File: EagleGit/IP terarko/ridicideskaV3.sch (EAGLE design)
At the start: 55 parts, among them IC1 74HC595N, IC2 74HC597N, Q3 32.768kHz

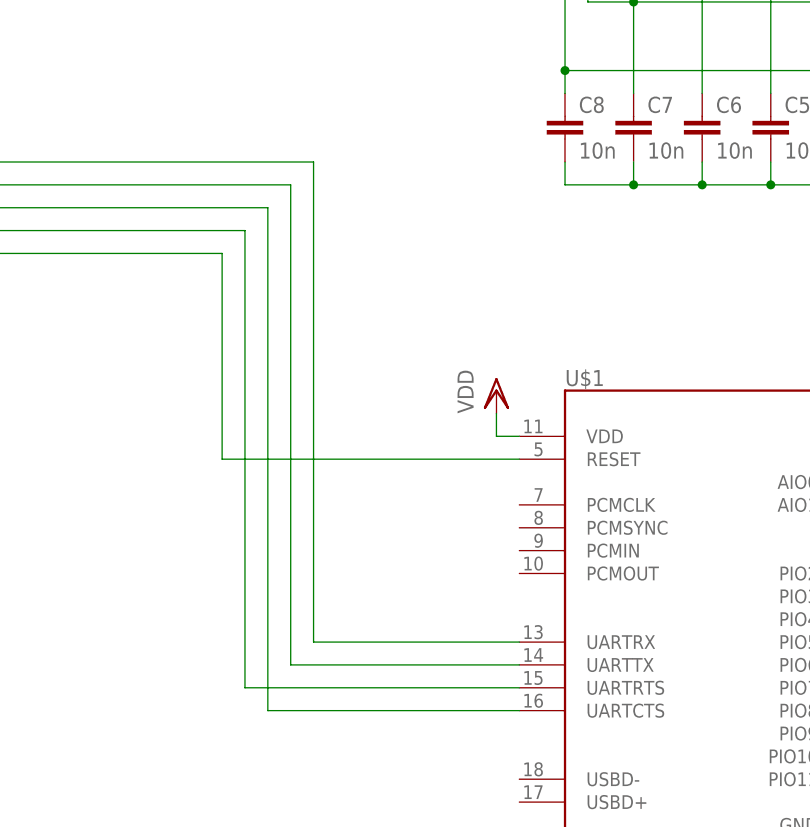
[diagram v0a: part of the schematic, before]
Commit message: Terarko: - chyba na ridici desce, byly prohozeny TX a RX privody k bluetooth modulu.
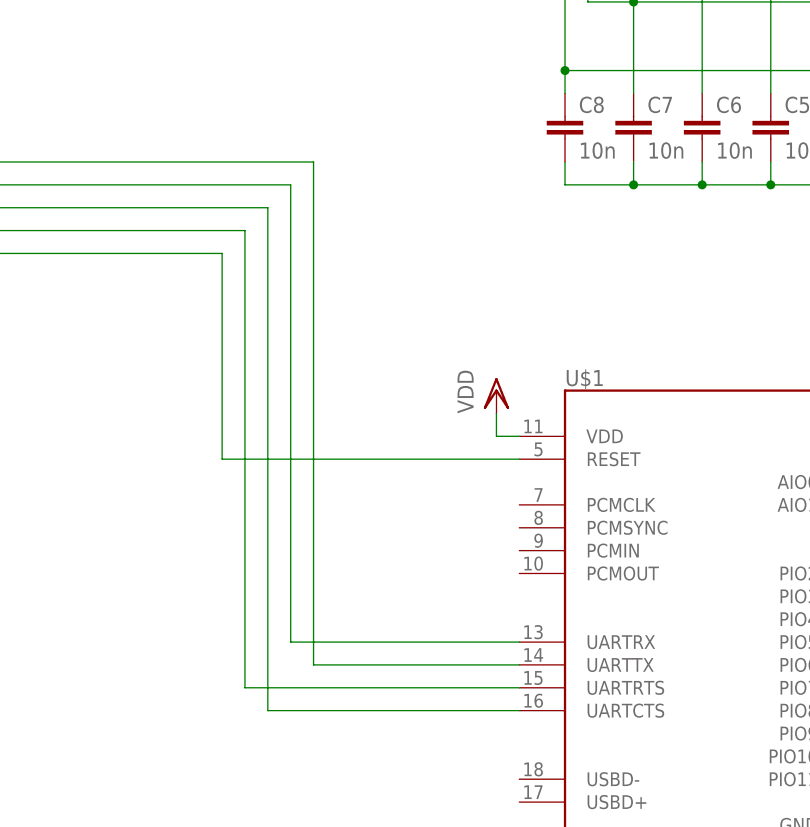
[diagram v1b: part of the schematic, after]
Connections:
- net N$47: now also U$1.UARTRX; no longer U$1.UARTTX
- net N$48: now also U$1.UARTTX; no longer U$1.UARTRX
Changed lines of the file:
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@@
 <?xml version="1.0" encoding="utf-8"?>
 <!DOCTYPE eagle SYSTEM "eagle.dtd">
-<eagle version="6.3">
+<eagle version="7.2.0">
 <drawing>
 <settings>
@@
 <grid distance="0.1" unitdist="inch" unit="inch" style="lines" multiple="1" display="no" altdistance="0.01" altunitdist="inch" altunit="inch"/>
 <layers>
-<layer number="1" name="Top" color="4" fill="1" visible="yes" active="no"/>
-<layer number="2" name="Route2" color="1" fill="3" visible="yes" active="no"/>
-<layer number="3" name="Route3" color="4" fill="3" visible="yes" active="no"/>
-<layer number="4" name="Route4" color="1" fill="4" visible="yes" active="no"/>
-<layer number="5" name="Route5" color="4" fill="4" visible="yes" active="no"/>
-<layer number="6" name="Route6" color="1" fill="8" visible="yes" active="no"/>
-<layer number="7" name="Route7" color="4" fill="8" visible="yes" active="no"/>
-<layer number="8" name="Route8" color="1" fill="2" visible="yes" active="no"/>
-<layer number="9" name="Route9" color="4" fill="2" visible="yes" active="no"/>
-<layer number="10" name="Route10" color="1" fill="7" visible="yes" active="no"/>
-<layer number="11" name="Route11" color="4" fill="7" visible="yes" active="no"/>
-<layer number="12" name="Route12" color="1" fill="5" visible="yes" active="no"/>
-<layer number="13" name="Route13" color="4" fill="5" visible="yes" active="no"/>
-<layer number="14" name="Route14" color="1" fill="6" visible="yes" active="no"/>
-<layer number="15" name="Route15" color="4" fill="6" visible="yes" active="no"/>
-<layer number="16" name="Bottom" color="1" fill="1" visible="yes" active="no"/>
-<layer number="17" name="Pads" color="2" fill="1" visible="yes" active="no"/>
-<layer number="18" name="Vias" color="2" fill="1" visible="yes" active="no"/>
-<layer number="19" name="Unrouted" color="6" fill="1" visible="yes" active="no"/>
-<layer number="20" name="Dimension" color="15" fill="1" visible="yes" active="no"/>
-<layer number="21" name="tPlace" color="7" fill="1" visible="yes" active="no"/>
-<layer number="22" name="bPlace" color="7" fill="1" visible="yes" active="no"/>
-<layer number="23" name="tOrigins" color="15" fill="1" visible="yes" active="no"/>
-<layer number="24" name="bOrigins" color="15" fill="1" visible="yes" active="no"/>
-<layer number="25" name="tNames" color="7" fill="1" visible="yes" active="no"/>
-<layer number="26" name="bNames" color="7" fill="1" visible="yes" active="no"/>
-<layer number="27" name="tValues" color="7" fill="1" visible="yes" active="no"/>
-<layer number="28" name="bValues" color="7" fill="1" visible="yes" active="no"/>
+<layer number="1" name="Top" color="4" fill="1" visible="no" active="no"/>
+<layer number="2" name="Route2" color="1" fill="3" visible="no" active="no"/>
+<layer number="3" name="Route3" color="4" fill="3" visible="no" active="no"/>
+<layer number="4" name="Route4" color="1" fill="4" visible="no" active="no"/>
+<layer number="5" name="Route5" color="4" fill="4" visible="no" active="no"/>
+<layer number="6" name="Route6" color="1" fill="8" visible="no" active="no"/>
+<layer number="7" name="Route7" color="4" fill="8" visible="no" active="no"/>
+<layer number="8" name="Route8" color="1" fill="2" visible="no" active="no"/>
+<layer number="9" name="Route9" color="4" fill="2" visible="no" active="no"/>
+<layer number="10" name="Route10" color="1" fill="7" visible="no" active="no"/>
+<layer number="11" name="Route11" color="4" fill="7" visible="no" active="no"/>
+<layer number="12" name="Route12" color="1" fill="5" visible="no" active="no"/>
+<layer number="13" name="Route13" color="4" fill="5" visible="no" active="no"/>
+<layer number="14" name="Route14" color="1" fill="6" visible="no" active="no"/>
+<layer number="15" name="Route15" color="4" fill="6" visible="no" active="no"/>
+<layer number="16" name="Bottom" color="1" fill="1" visible="no" active="no"/>
+<layer number="17" name="Pads" color="2" fill="1" visible="no" active="no"/>
+<layer number="18" name="Vias" color="2" fill="1" visible="no" active="no"/>
+<layer number="19" name="Unrouted" color="6" fill="1" visible="no" active="no"/>
+<layer number="20" name="Dimension" color="15" fill="1" visible="no" active="no"/>
+<layer number="21" name="tPlace" color="7" fill="1" visible="no" active="no"/>
+<layer number="22" name="bPlace" color="7" fill="1" visible="no" active="no"/>
+<layer number="23" name="tOrigins" color="15" fill="1" visible="no" active="no"/>
+<layer number="24" name="bOrigins" color="15" fill="1" visible="no" active="no"/>
+<layer number="25" name="tNames" color="7" fill="1" visible="no" active="no"/>
+<layer number="26" name="bNames" color="7" fill="1" visible="no" active="no"/>
+<layer number="27" name="tValues" color="7" fill="1" visible="no" active="no"/>
+<layer number="28" name="bValues" color="7" fill="1" visible="no" active="no"/>
 <layer number="29" name="tStop" color="7" fill="3" visible="no" active="no"/>
 <layer number="30" name="bStop" color="7" fill="6" visible="no" active="no"/>
@@
 <layer number="35" name="tGlue" color="7" fill="4" visible="no" active="no"/>
 <layer number="36" name="bGlue" color="7" fill="5" visible="no" active="no"/>
-<layer number="37" name="tTest" color="7" fill="1" visible="yes" active="no"/>
-<layer number="38" name="bTest" color="7" fill="1" visible="yes" active="no"/>
+<layer number="37" name="tTest" color="7" fill="1" visible="no" active="no"/>
+<layer number="38" name="bTest" color="7" fill="1" visible="no" active="no"/>
 <layer number="39" name="tKeepout" color="4" fill="11" visible="no" active="no"/>
 <layer number="40" name="bKeepout" color="1" fill="11" visible="no" active="no"/>
@@
 <layer number="44" name="Drills" color="7" fill="1" visible="no" active="no"/>
 <layer number="45" name="Holes" color="7" fill="1" visible="no" active="no"/>
-<layer number="46" name="Milling" color="3" fill="1" visible="yes" active="no"/>
-<layer number="47" name="Measures" color="7" fill="1" visible="yes" active="no"/>
-<layer number="48" name="Document" color="7" fill="1" visible="yes" active="no"/>
-<layer number="49" name="Reference" color="7" fill="1" visible="yes" active="no"/>
-<layer number="50" name="dxf" color="7" fill="1" visible="yes" active="no"/>
-<layer number="51" name="tDocu" color="7" fill="1" visible="yes" active="no"/>
-<layer number="52" name="bDocu" color="7" fill="1" visible="yes" active="no"/>
-<layer number="53" name="tGND_GNDA" color="7" fill="9" visible="yes" active="no"/>
-<layer number="54" name="bGND_GNDA" color="1" fill="9" visible="yes" active="no"/>
-<layer number="56" name="wert" color="7" fill="1" visible="yes" active="no"/>
-<layer number="57" name="tCAD" color="7" fill="1" visible="yes" active="no"/>
+<layer number="46" name="Milling" color="3" fill="1" visible="no" active="no"/>
+<layer number="47" name="Measures" color="7" fill="1" visible="no" active="no"/>
+<layer number="48" name="Document" color="7" fill="1" visible="no" active="no"/>
+<layer number="49" name="Reference" color="7" fill="1" visible="no" active="no"/>
+<layer number="50" name="dxf" color="7" fill="1" visible="no" active="no"/>
+<layer number="51" name="tDocu" color="7" fill="1" visible="no" active="no"/>
+<layer number="52" name="bDocu" color="7" fill="1" visible="no" active="no"/>
+<layer number="53" name="tGND_GNDA" color="7" fill="9" visible="no" active="no"/>
+<layer number="54" name="bGND_GNDA" color="1" fill="9" visible="no" active="no"/>
+<layer number="56" name="wert" color="7" fill="1" visible="no" active="no"/>
+<layer number="57" name="tCAD" color="7" fill="1" visible="no" active="no"/>
 <layer number="90" name="Modules" color="5" fill="1" visible="yes" active="yes"/>
 <layer number="91" name="Nets" color="2" fill="1" visible="yes" active="yes"/>
@@
 <pinref part="IO1" gate="G$1" pin="PD5"/>
 <wire x1="116.84" y1="15.24" x2="182.88" y2="15.24" width="0.1524" layer="91"/>
-<wire x1="182.88" y1="15.24" x2="182.88" y2="-38.1" width="0.1524" layer="91"/>
-<pinref part="U$1" gate="G$1" pin="UARTTX"/>
-<wire x1="182.88" y1="-38.1" x2="208.28" y2="-38.1" width="0.1524" layer="91"/>
+<wire x1="182.88" y1="15.24" x2="182.88" y2="-35.56" width="0.1524" layer="91"/>
+<pinref part="U$1" gate="G$1" pin="UARTRX"/>
+<wire x1="208.28" y1="-35.56" x2="182.88" y2="-35.56" width="0.1524" layer="91"/>
 </segment>
 </net>
@@
 <pinref part="IO1" gate="G$1" pin="PD6"/>
 <wire x1="116.84" y1="17.78" x2="185.42" y2="17.78" width="0.1524" layer="91"/>
-<wire x1="185.42" y1="17.78" x2="185.42" y2="-35.56" width="0.1524" layer="91"/>
-<pinref part="U$1" gate="G$1" pin="UARTRX"/>
-<wire x1="185.42" y1="-35.56" x2="208.28" y2="-35.56" width="0.1524" layer="91"/>
-</segment>
-</net>
+<wire x1="185.42" y1="17.78" x2="185.42" y2="-38.1" width="0.1524" layer="91"/>
+<pinref part="U$1" gate="G$1" pin="UARTTX"/>
+<wire x1="208.28" y1="-38.1" x2="185.42" y2="-38.1" width="0.1524" layer="91"/>
+</segment>
+</net>

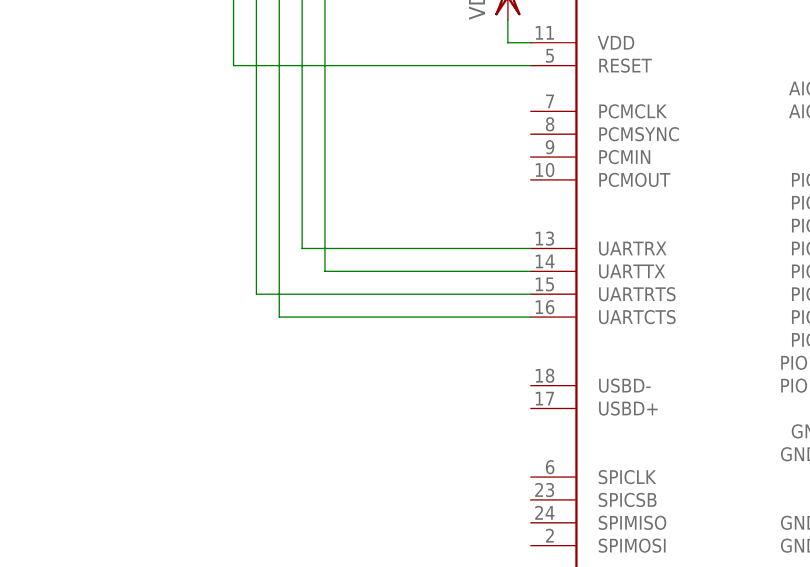
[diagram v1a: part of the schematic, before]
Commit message: Terarko: - do cesty Rx, CTS pridany 1k rezistory
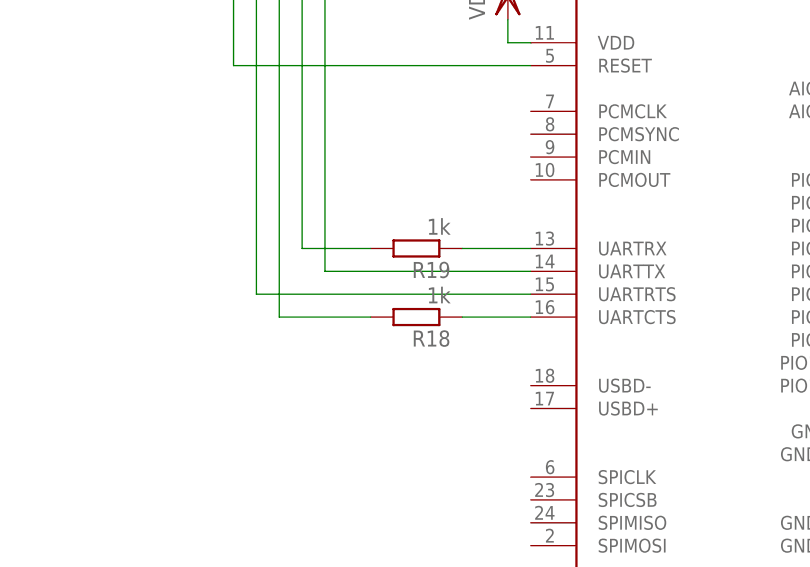
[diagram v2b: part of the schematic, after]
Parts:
- added R18, R19: 1k, rcl:R-EU_0207/12
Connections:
- new net N$42: R19.1, U$1.UARTRX
- new net N$65: R18.1, U$1.UARTCTS
- net N$47: now also R19.2; no longer U$1.UARTRX
- net N$63: now also R18.2; no longer U$1.UARTCTS
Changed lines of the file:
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@@
 <part name="C19" library="rcl" deviceset="C-EU" device="C0805" value="10n"/>
 <part name="C20" library="rcl" deviceset="C-EU" device="C0805" value="10n"/>
+<part name="R18" library="rcl" deviceset="R-EU_" device="0207/12" value="1k"/>
+<part name="R19" library="rcl" deviceset="R-EU_" device="0207/12" value="1k"/>
 </parts>
 <sheets>
@@
 <instance part="C19" gate="G$1" x="2.54" y="203.2"/>
 <instance part="C20" gate="G$1" x="12.7" y="203.2"/>
+<instance part="R18" gate="G$1" x="195.58" y="-43.18" rot="R180"/>
+<instance part="R19" gate="G$1" x="195.58" y="-35.56" rot="R180"/>
 </instances>
 <busses>
@@
 <wire x1="116.84" y1="15.24" x2="182.88" y2="15.24" width="0.1524" layer="91"/>
 <wire x1="182.88" y1="15.24" x2="182.88" y2="-35.56" width="0.1524" layer="91"/>
-<pinref part="U$1" gate="G$1" pin="UARTRX"/>
-<wire x1="208.28" y1="-35.56" x2="182.88" y2="-35.56" width="0.1524" layer="91"/>
+<pinref part="R19" gate="G$1" pin="2"/>
+<wire x1="190.5" y1="-35.56" x2="182.88" y2="-35.56" width="0.1524" layer="91"/>
 </segment>
 </net>
@@
 <wire x1="116.84" y1="12.7" x2="180.34" y2="12.7" width="0.1524" layer="91"/>
 <wire x1="180.34" y1="12.7" x2="180.34" y2="-43.18" width="0.1524" layer="91"/>
-<pinref part="U$1" gate="G$1" pin="UARTCTS"/>
-<wire x1="180.34" y1="-43.18" x2="208.28" y2="-43.18" width="0.1524" layer="91"/>
+<wire x1="180.34" y1="-43.18" x2="190.5" y2="-43.18" width="0.1524" layer="91"/>
+<pinref part="R18" gate="G$1" pin="2"/>
 </segment>
 </net>
@@
 </segment>
 </net>
+<net name="N$42" class="0">
+<segment>
+<pinref part="U$1" gate="G$1" pin="UARTRX"/>
+<wire x1="208.28" y1="-35.56" x2="200.66" y2="-35.56" width="0.1524" layer="91"/>
+<pinref part="R19" gate="G$1" pin="1"/>
+</segment>
+</net>
+<net name="N$65" class="0">
+<segment>
+<pinref part="U$1" gate="G$1" pin="UARTCTS"/>
+<pinref part="R18" gate="G$1" pin="1"/>
+<wire x1="200.66" y1="-43.18" x2="208.28" y2="-43.18" width="0.1524" layer="91"/>
+</segment>
+</net>

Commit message: VDDA - odpojeno od napajeni, na desce discovery kitu je filtrovana hodnota
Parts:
- removed C20: 10n, rcl:C-EUC0805
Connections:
- net GND: no longer C20.2
- net VDD_P: no longer C20.1, IO1.VDDA
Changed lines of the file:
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@@
 <part name="C18" library="rcl" deviceset="C-EU" device="C0805" value="10n"/>
 <part name="C19" library="rcl" deviceset="C-EU" device="C0805" value="10n"/>
-<part name="C20" library="rcl" deviceset="C-EU" device="C0805" value="10n"/>
 <part name="R18" library="rcl" deviceset="R-EU_" device="0207/12" value="1k"/>
 <part name="R19" library="rcl" deviceset="R-EU_" device="0207/12" value="1k"/>
@@
 <instance part="C18" gate="G$1" x="-7.62" y="203.2"/>
 <instance part="C19" gate="G$1" x="2.54" y="203.2"/>
-<instance part="C20" gate="G$1" x="12.7" y="203.2"/>
 <instance part="R18" gate="G$1" x="195.58" y="-43.18" rot="R180"/>
 <instance part="R19" gate="G$1" x="195.58" y="-35.56" rot="R180"/>
@@
 <wire x1="2.54" y1="195.58" x2="2.54" y2="198.12" width="0.1524" layer="91"/>
 <junction x="-7.62" y="195.58"/>
-<pinref part="C20" gate="G$1" pin="2"/>
-<wire x1="12.7" y1="198.12" x2="12.7" y2="195.58" width="0.1524" layer="91"/>
-<wire x1="12.7" y1="195.58" x2="2.54" y2="195.58" width="0.1524" layer="91"/>
-<junction x="2.54" y="195.58"/>
 </segment>
 </net>
@@
 <segment>
 <wire x1="71.12" y1="48.26" x2="58.42" y2="48.26" width="0.1524" layer="91"/>
-<wire x1="71.12" y1="33.02" x2="58.42" y2="33.02" width="0.1524" layer="91"/>
-<wire x1="58.42" y1="33.02" x2="58.42" y2="38.1" width="0.1524" layer="91"/>
 <wire x1="58.42" y1="38.1" x2="58.42" y2="43.18" width="0.1524" layer="91"/>
 <wire x1="58.42" y1="43.18" x2="58.42" y2="48.26" width="0.1524" layer="91"/>
 <wire x1="71.12" y1="38.1" x2="58.42" y2="38.1" width="0.1524" layer="91"/>
-<junction x="58.42" y="38.1"/>
 <wire x1="71.12" y1="43.18" x2="58.42" y2="43.18" width="0.1524" layer="91"/>
 <junction x="58.42" y="43.18"/>
@@
 <pinref part="IO1" gate="G$1" pin="VDD"/>
 <pinref part="IO1" gate="G$1" pin="VDDIO_2"/>
-<pinref part="IO1" gate="G$1" pin="VDDA"/>
 <pinref part="C9" gate="G$1" pin="1"/>
 <wire x1="25.4" y1="43.18" x2="25.4" y2="48.26" width="0.1524" layer="91"/>
@@
 <junction x="-7.62" y="208.28"/>
 <label x="-7.62" y="213.36" size="1.778" layer="95" rot="R90"/>
-<wire x1="2.54" y1="208.28" x2="12.7" y2="208.28" width="0.1524" layer="91"/>
-<junction x="2.54" y="208.28"/>
-<pinref part="C20" gate="G$1" pin="1"/>
-<wire x1="12.7" y1="208.28" x2="12.7" y2="205.74" width="0.1524" layer="91"/>
-</segment>
-</net>
+</segment>
+</net>

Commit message: Terarko: -na DPS pridan napajeci konektor -na DPS pridan konektor SPI -opraveny vsechny cesty
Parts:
- added CON5: (no value), con-harting:CON06
- added R20: 150R, rcl:R-EU_R0805
- added X1: (no value), con-conrad:733980-62
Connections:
- new net N$70: IO1.PC7|MISO, R20.1
- new net N$71: CON5.1, R20.2
- new net N$72: CON5.3, IO1.PC6|MOSI
- new net N$73: CON5.5, IO1.PC5|SCK
- net GND: now also CON5.2, CON5.4, X1.2, X1.3
- net VDD: now also X1.1
- net VDD_P: now also CON5.6
